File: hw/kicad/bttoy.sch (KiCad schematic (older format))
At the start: 35 parts, among them J1 USB-micro-b, J2 HC-07_BLUETOOTH, J3 ARM_10PIN, P1 +9V_DBG, P2 M1+, P3 M1-, P4 M2+, P5 M2-, SW1 SPDT (Apem MHSS1105), U1 AAT3221/MIC5504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

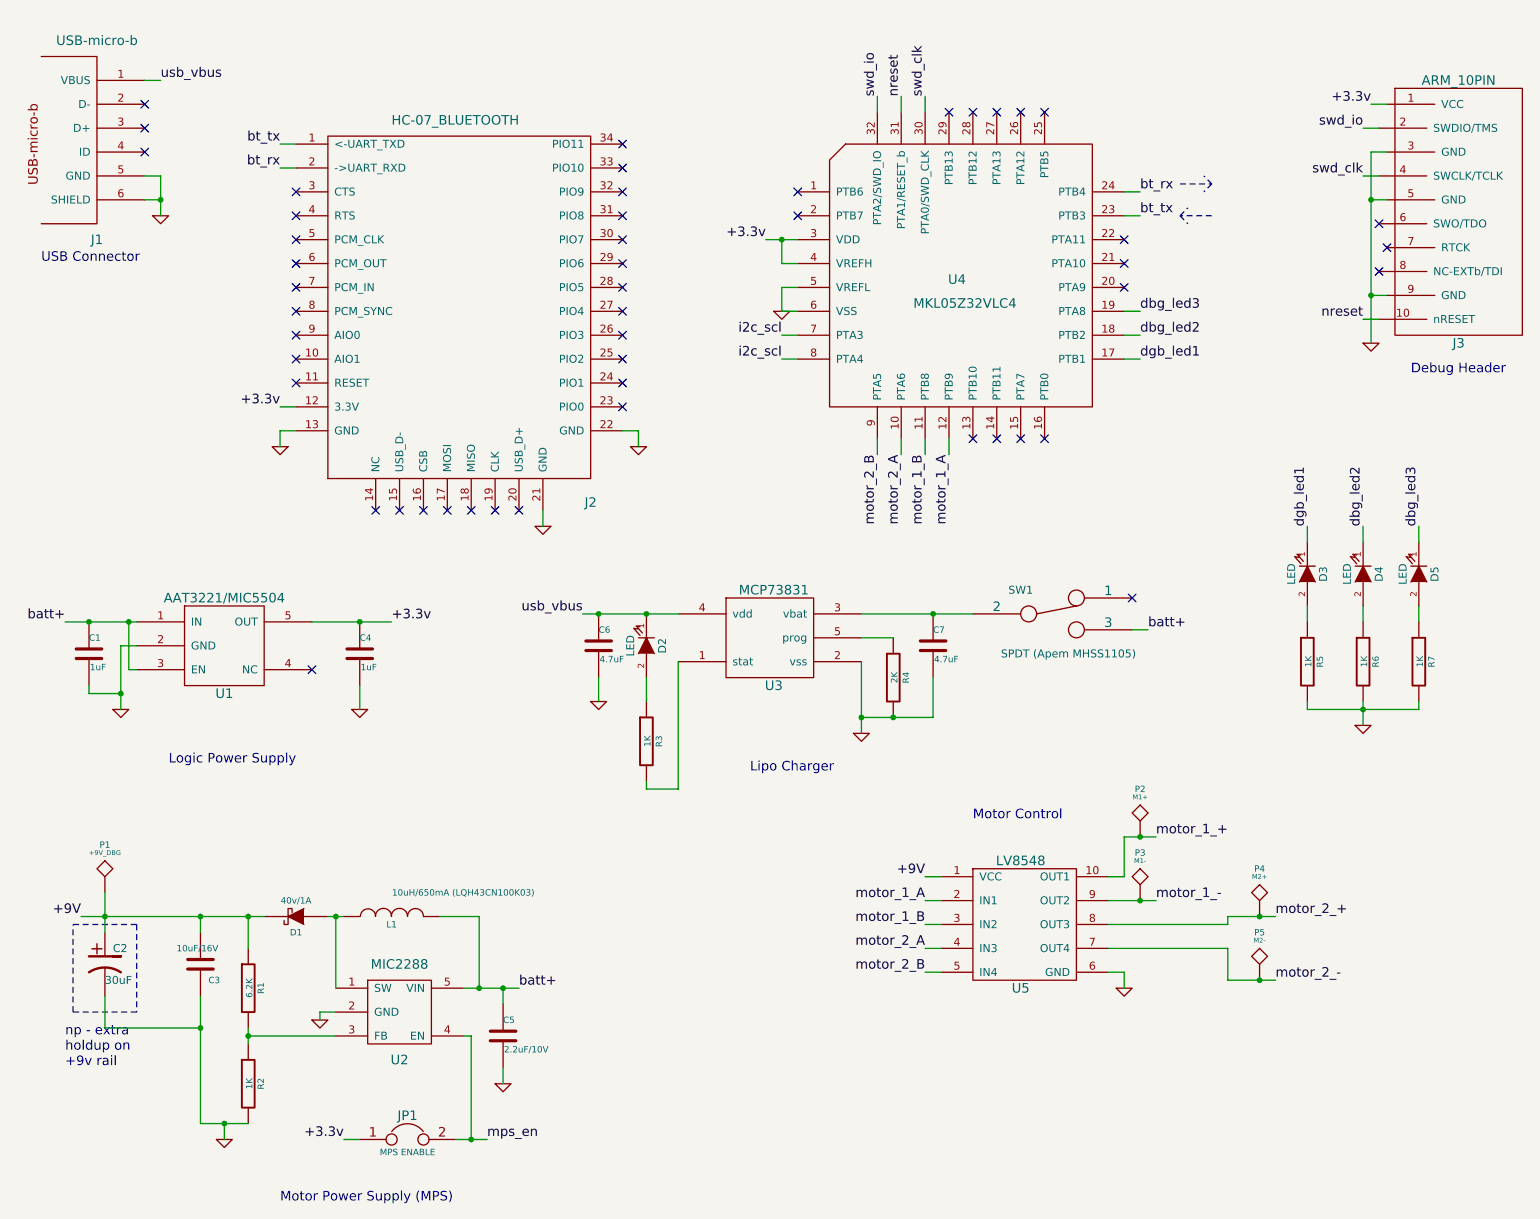
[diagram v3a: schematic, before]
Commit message: - add bom, add acc. connections, reload parts on pcb
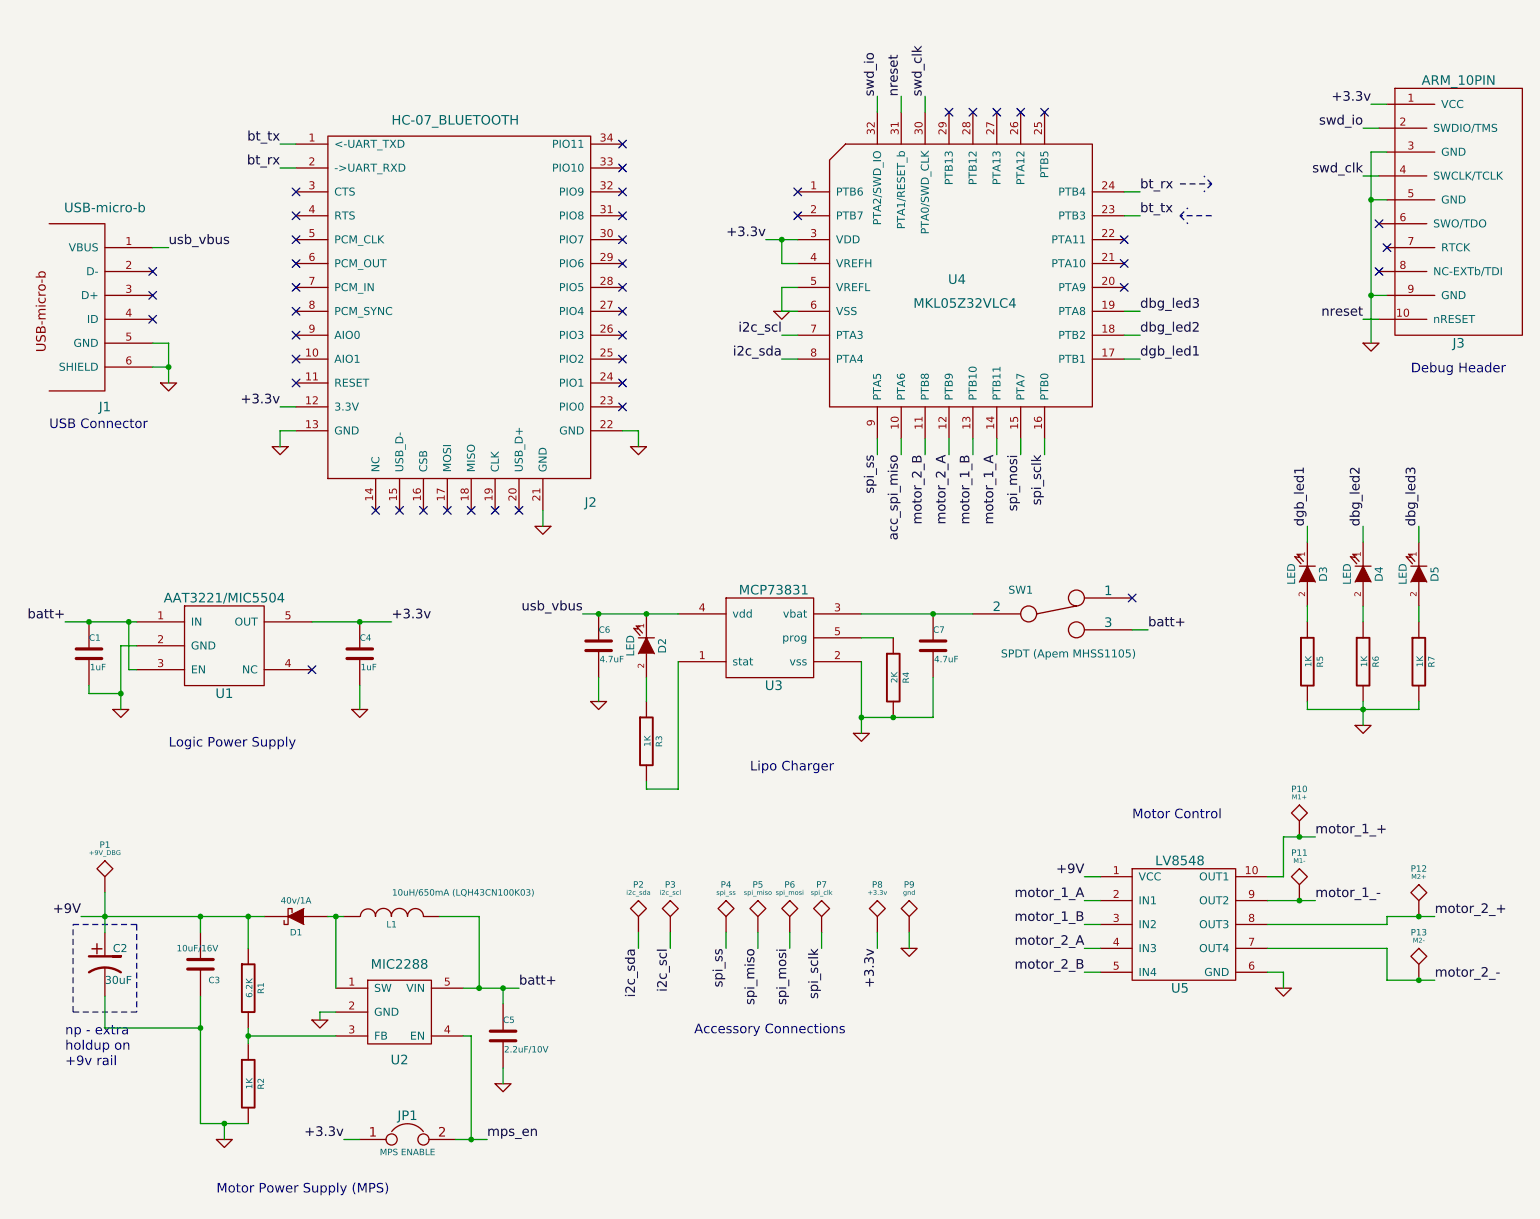
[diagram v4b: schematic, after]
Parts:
- added P2: i2c_sda, kicadlib:TEST_0.100, symbol TST
- added P3: i2c_scl, kicadlib:TEST_0.100, symbol TST
- added P4: spi_ss, kicadlib:TEST_0.100, symbol TST
- added P5: spi_miso, kicadlib:TEST_0.100, symbol TST
- added P6: spi_mosi, kicadlib:TEST_0.100, symbol TST
- added P7: spi_clk, kicadlib:TEST_0.100, symbol TST
- added P8: +3.3v, kicadlib:TEST_0.100, symbol TST
- added P9: gnd, kicadlib:TEST_0.100, symbol TST
- renumbered P2 to P10, P3 to P11, P4 to P12, P5 to P13
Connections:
- net +3.3v: now also P8.1
- net GND: now also P9.1
- net i2c_scl: now also P3.1; no longer U4.8 (PTA4)
- net motor_1_A: now also U4.14 (PTB11); no longer U4.12 (PTB9)
- net motor_1_B: now also U4.13 (PTB10); no longer U4.11 (PTB8)
- net motor_2_A: now also U4.12 (PTB9); no longer U4.10 (PTA6)
- net motor_2_B: now also U4.11 (PTB8); no longer U4.9 (PTA5)
- net spi_mosi: now reaches U4.15 (PTA7)
- net spi_mosi: now also P6.1
- net spi_sclk: now reaches U4.16 (PTB0)
- net spi_sclk: now also P7.1
- new net acc_spi_miso: U4.10 (PTA6)
- new net i2c_sda: P2.1, U4.8 (PTA4)
- new net spi_miso: P5.1
- new net spi_ss: P4.1, U4.9 (PTA5)
- no-connect marks 50 -> 46
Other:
- note added: "Accessory Connections"
- moved on the sheet: J1, P10, P11, P12, P13, U5

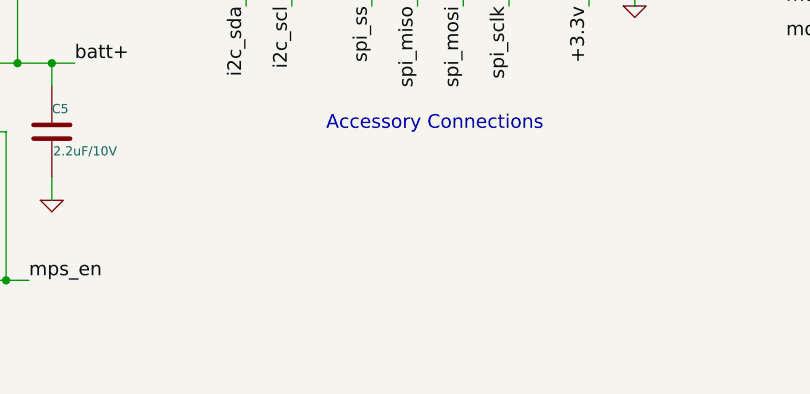
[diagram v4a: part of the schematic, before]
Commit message: tune up schematic a bit more, and start positioning footprints on pcb
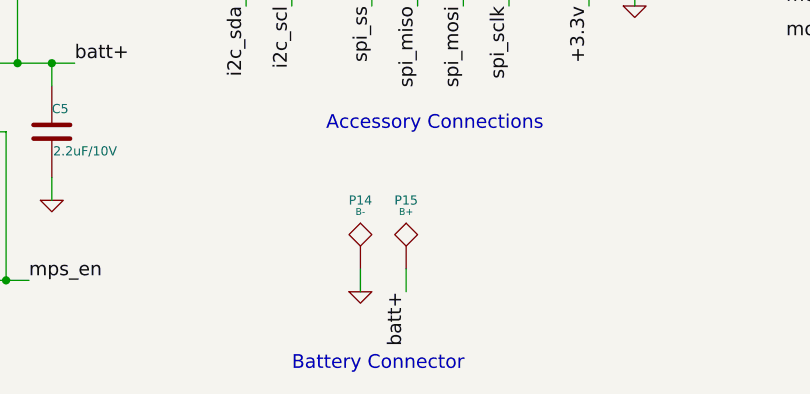
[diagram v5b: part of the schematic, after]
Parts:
- added P14: B-, kicadlib:TEST_0.100, symbol TST
- added P15: B+, kicadlib:TEST_0.100, symbol TST
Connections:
- net GND: now also P14.1
- net batt+: now also P15.1
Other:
- note added: "Battery Connector"
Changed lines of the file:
@@
 Text Notes 4850 6800 0    60   ~ 0
 Accessory Connections
+Text Label 5200 7500 3    60   ~ 0
+batt+
+$Comp
+L GND #PWR017
+U 1 1 5536D437
+P 5000 7500
+F 0 "#PWR017" H 5000 7500 30  0001 C CNN
+F 1 "GND" H 5000 7430 30  0001 C CNN
+F 2 "" H 5000 7500 60  0000 C CNN
+F 3 "" H 5000 7500 60  0000 C CNN
+	1    5000 7500
+	1    0    0    -1
+$EndComp
+$Comp
+L TST P14
+U 1 1 5536D519
+P 5000 7400
+F 0 "P14" H 5000 7700 40  0000 C CNN
+F 1 "B-" H 5000 7650 30  0000 C CNN
+F 2 "kicadlib:TEST_0.100" H 5000 7400 60  0001 C CNN
+F 3 "" H 5000 7400 60  0000 C CNN
+	1    5000 7400
+	1    0    0    -1
+$EndComp
+$Comp
+L TST P15
+U 1 1 5536D57D
+P 5200 7400
+F 0 "P15" H 5200 7700 40  0000 C CNN
+F 1 "B+" H 5200 7650 30  0000 C CNN
+F 2 "kicadlib:TEST_0.100" H 5200 7400 60  0001 C CNN
+F 3 "" H 5200 7400 60  0000 C CNN
+	1    5200 7400
+	1    0    0    -1
+$EndComp
+Wire Wire Line
+	5000 7400 5000 7500
+Wire Wire Line
+	5200 7500 5200 7400
+Text Notes 4700 7850 0    60   ~ 0
+Battery Connector
 $EndSCHEMATC

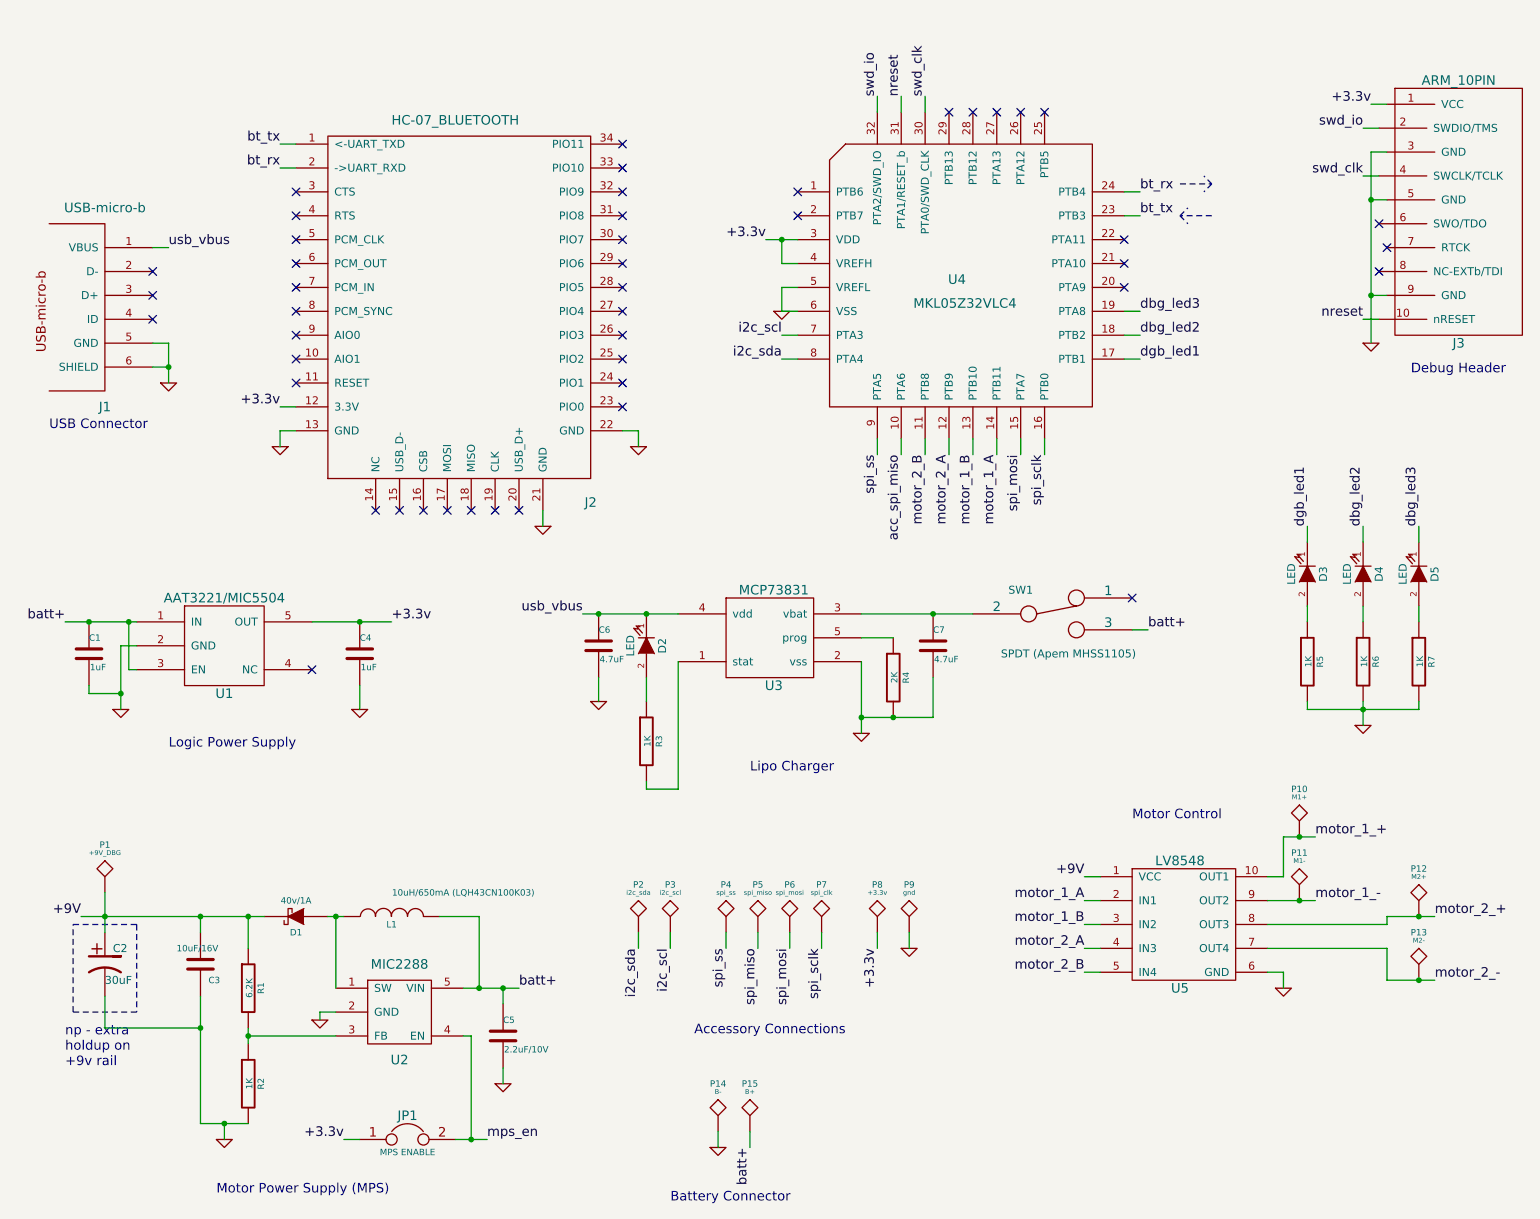
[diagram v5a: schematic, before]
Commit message: mps and dbg led's laid out
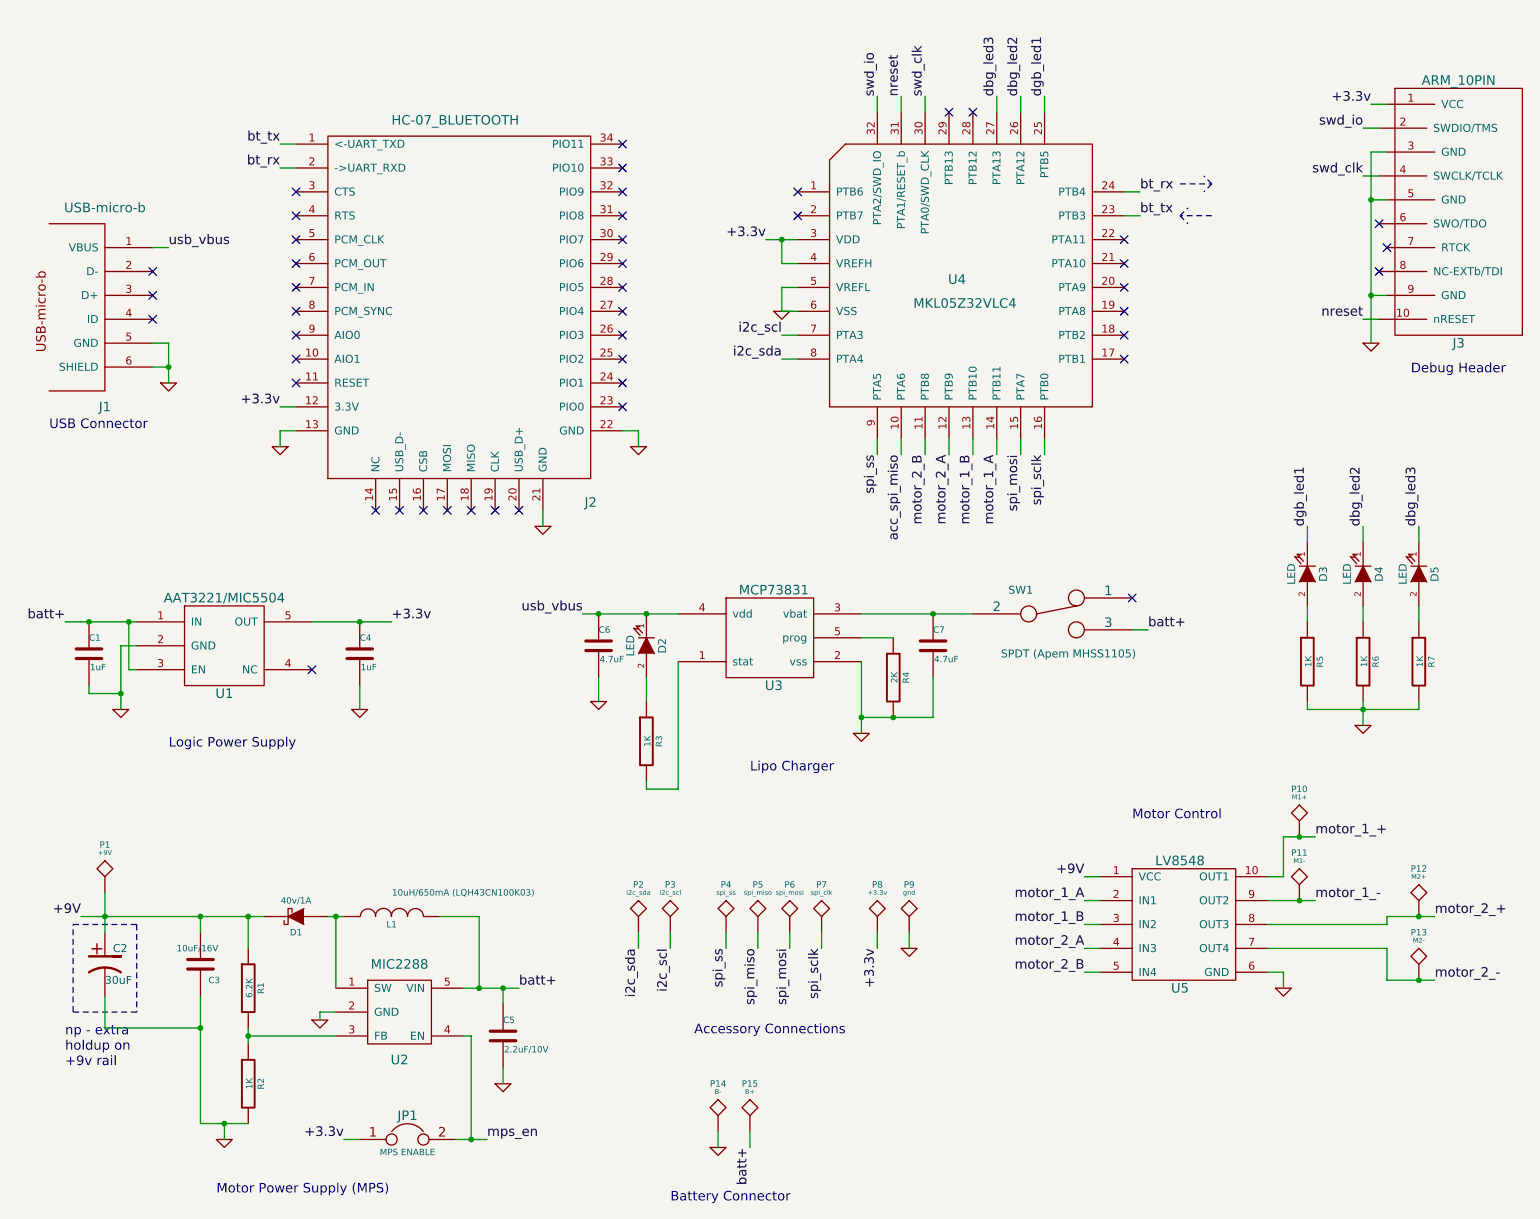
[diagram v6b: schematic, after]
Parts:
- P1: value +9V_DBG -> +9V
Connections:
- net dbg_led2: now also U4.26 (PTA12); no longer U4.18 (PTB2)
- net dbg_led3: now also U4.27 (PTA13); no longer U4.19 (PTA8)
- net dgb_led1: now also U4.25 (PTB5); no longer U4.17 (PTB1)
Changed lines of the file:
@@
 P 1150 5900
 F 0 "P1" H 1150 6200 40  0000 C CNN
-F 1 "+9V_DBG" H 1150 6150 30  0000 C CNN
+F 1 "+9V" H 1150 6150 30  0000 C CNN
 F 2 "kicadlib:TEST_0.100" H 1150 5900 60  0001 C CNN
 F 3 "" H 1150 5900 60  0000 C CNN
@@
 Text Label 9400 3600 1    60   ~ 0
 dbg_led3
-Text Label 7650 2550 0    60   ~ 0
+Text Label 7050 900  1    60   ~ 0
 dgb_led1
-Text Label 7650 2400 0    60   ~ 0
+Text Label 6900 900  1    60   ~ 0
 dbg_led2
-Text Label 7650 2250 0    60   ~ 0
+Text Label 6750 900  1    60   ~ 0
 dbg_led3
 Wire Wire Line
-	7650 2250 7550 2250
-Wire Wire Line
-	7550 2400 7650 2400
-Wire Wire Line
-	7650 2550 7550 2550
+	6750 900  6750 1000
+Wire Wire Line
+	6900 1000 6900 900
+Wire Wire Line
+	7050 900  7050 1000
 NoConn ~ 7550 2100
 NoConn ~ 7550 1950
 NoConn ~ 7550 1800
-NoConn ~ 7050 1000
-NoConn ~ 6900 1000
-NoConn ~ 6750 1000
 NoConn ~ 6600 1000
 NoConn ~ 6450 1000
@@
 Text Notes 4700 7850 0    60   ~ 0
 Battery Connector
+NoConn ~ 7550 2250
+NoConn ~ 7550 2400
+NoConn ~ 7550 2550
 $EndSCHEMATC
